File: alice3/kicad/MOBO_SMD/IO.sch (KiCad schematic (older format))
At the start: 31 parts, among them CON1 MicroSD, P2 UART1, P3 USB_OTG, SW2 SOFT RESET, U1 STM32F415RG, Y2 16MHz, Y3 32.768KHz

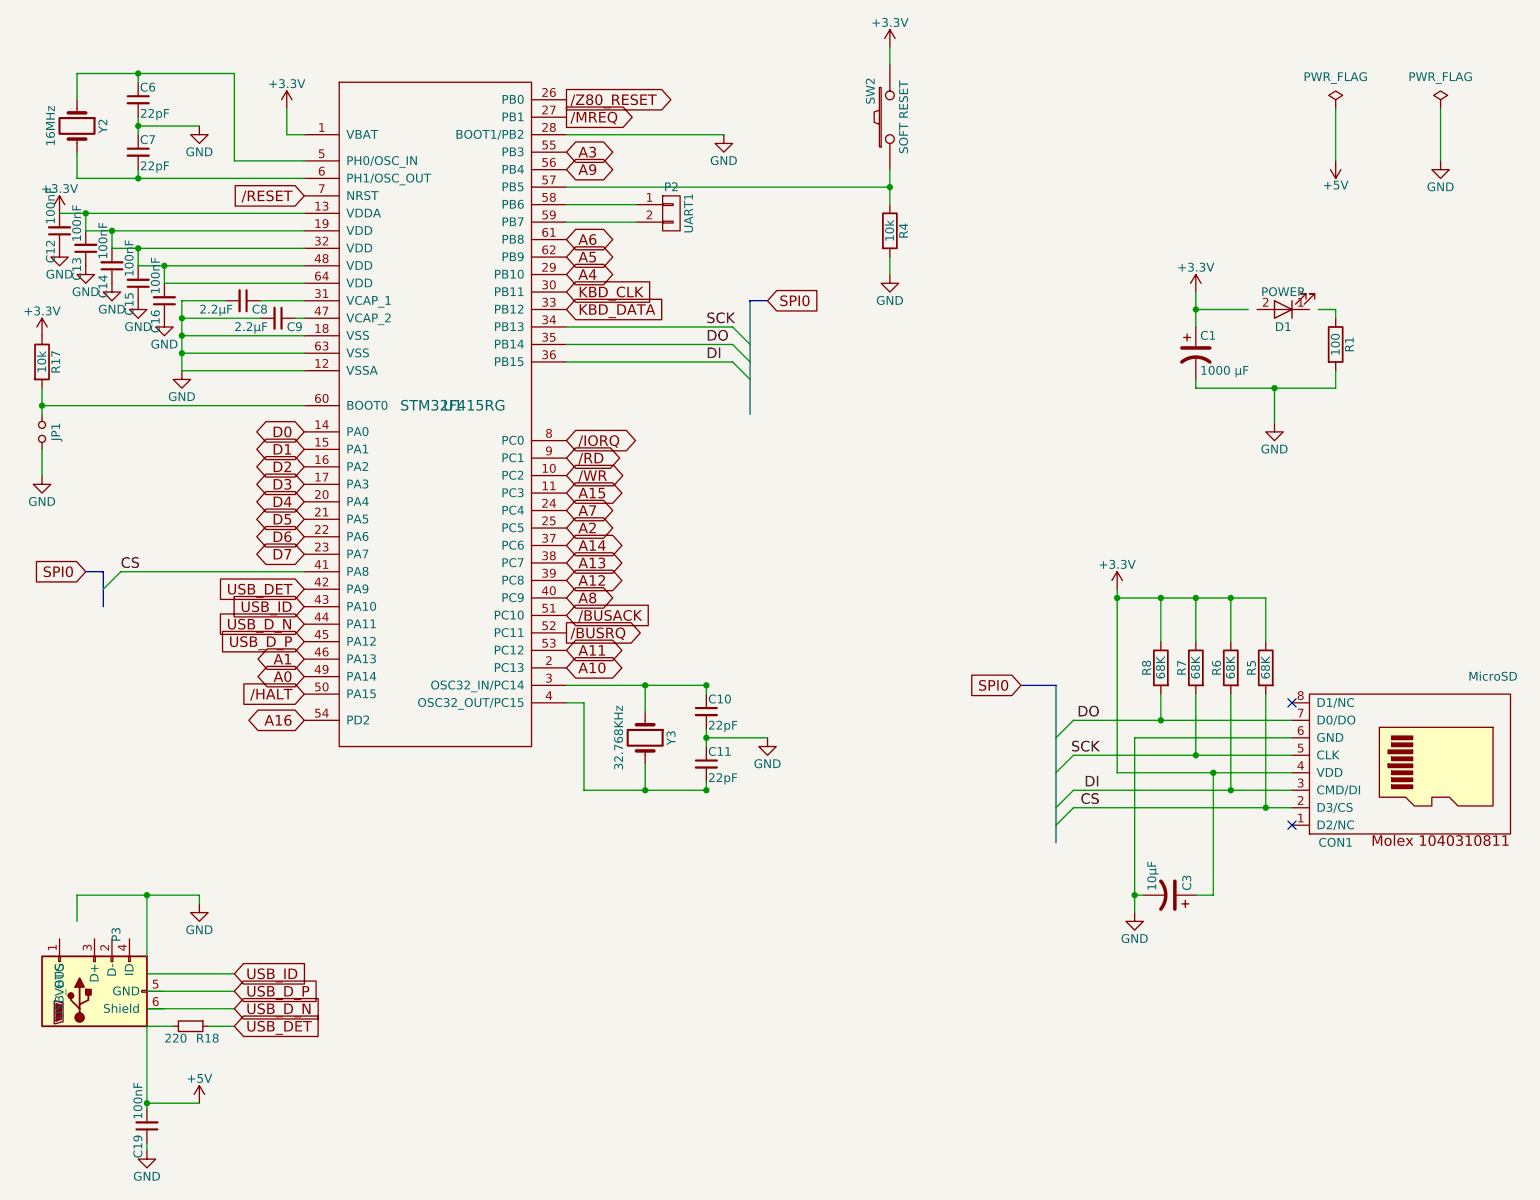
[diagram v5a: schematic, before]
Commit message: Stab at full PCB
replace DIP36 128KB RAM with TSOP44 512KB RAM
change footprints for many components to SMD
sample PCB layout
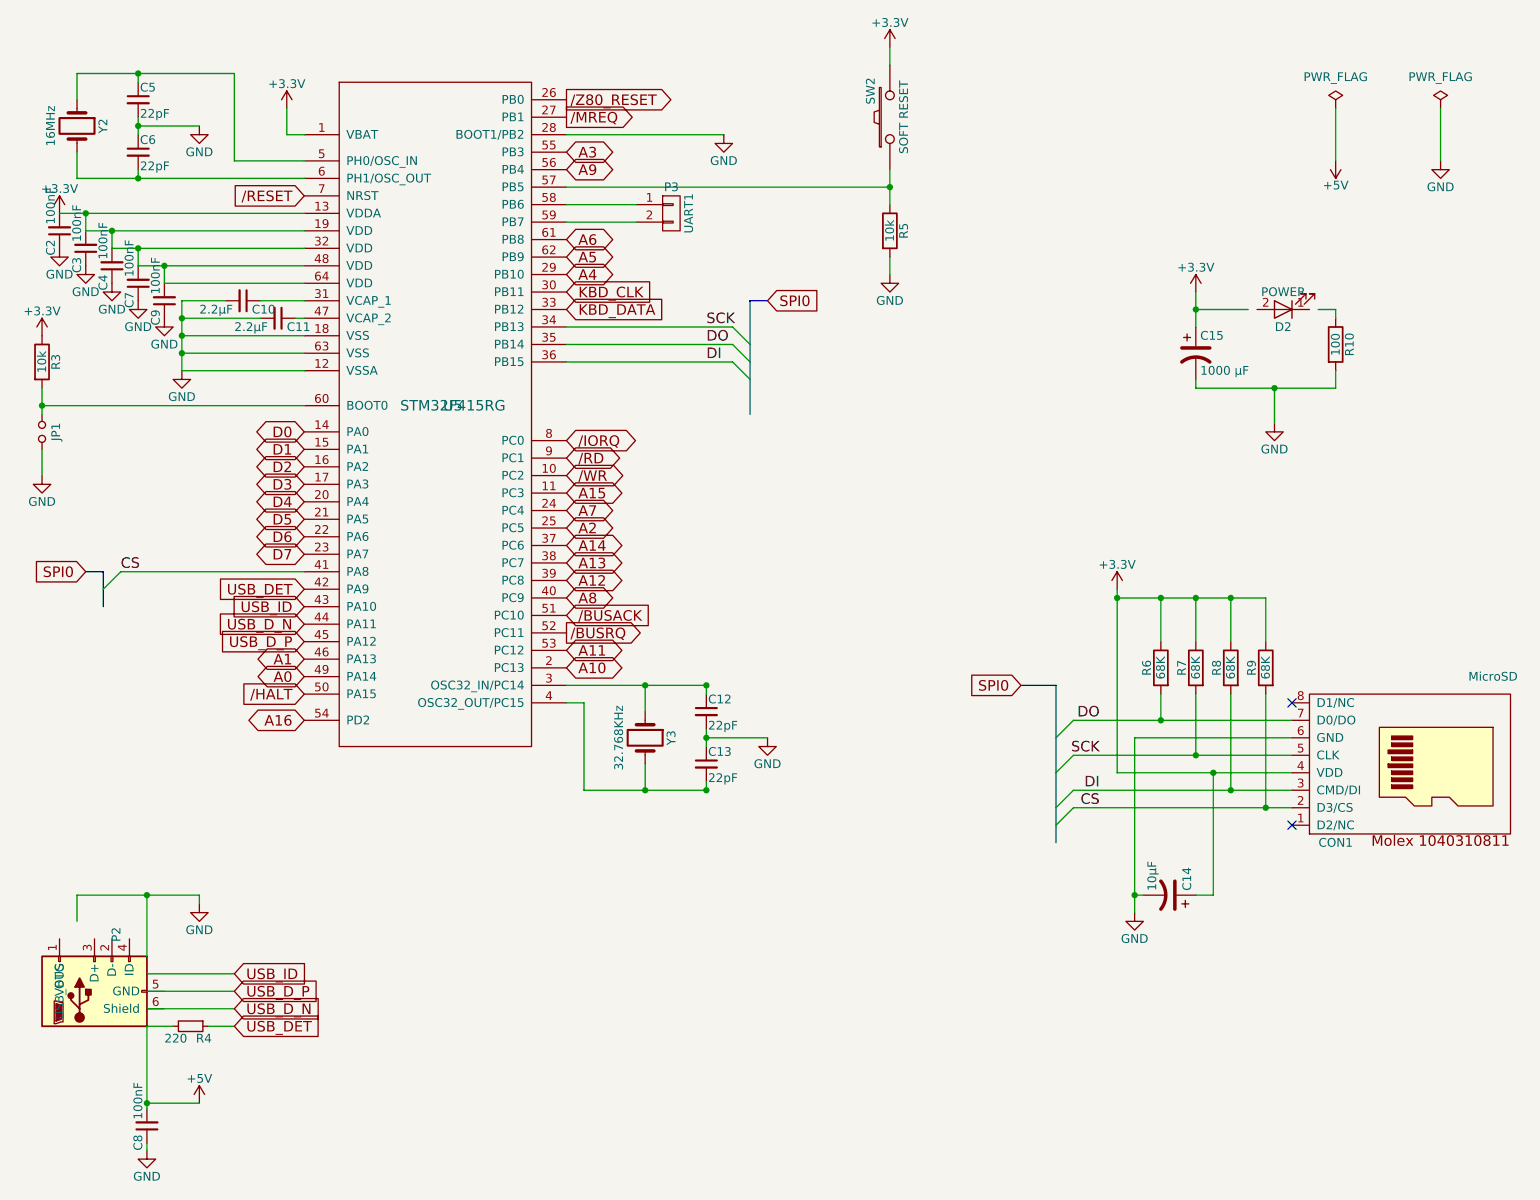
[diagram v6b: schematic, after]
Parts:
- C10: renamed from C8; footprint (none) -> Capacitors_SMD:C_0805
- C11: renamed from C9; footprint (none) -> Capacitors_SMD:C_0805
- C12: renamed from C10; footprint (none) -> Capacitors_SMD:C_0805
- C13: renamed from C11; footprint (none) -> Capacitors_SMD:C_0805
- C2: renamed from C12; footprint (none) -> Capacitors_SMD:C_0805
- C3: renamed from C13; footprint (none) -> Capacitors_SMD:C_0805
- C4: renamed from C14; footprint (none) -> Capacitors_SMD:C_0805
- C5: renamed from C6; footprint (none) -> Capacitors_SMD:C_0805
- C6: renamed from C7; footprint (none) -> Capacitors_SMD:C_0805
- C7: renamed from C15; footprint (none) -> Capacitors_SMD:C_0805
- C8: renamed from C19; footprint (none) -> Capacitors_SMD:C_0805
- C9: renamed from C16; footprint (none) -> Capacitors_SMD:C_0805
- CON1: footprint (none) -> microsd:microsd_socket
- D2: renamed from D1; footprint LEDs:LED-5MM -> LEDs:LED_0805
- JP1: footprint (none) -> Pin_Headers:Pin_Header_Straight_1x02
- P2: renamed from P3; footprint snapeda_conn:10118192-0001LF -> microusb:10118192-0001LF
- P3: renamed from P2; footprint (none) -> Pin_Headers:Pin_Header_Straight_1x02
- R10: renamed from R1; footprint Resistors_ThroughHole:Resistor_Horizontal_RM10mm -> Resistors_SMD:R_0805
- R3: renamed from R17; footprint Resistors_ThroughHole:Resistor_Horizontal_RM10mm -> Resistors_SMD:R_0805
- R4: renamed from R18; footprint (none) -> Resistors_SMD:R_0805
- R5: renamed from R4; footprint Resistors_ThroughHole:Resistor_Horizontal_RM10mm -> Resistors_SMD:R_0805
- R6: renamed from R8; footprint Resistors_ThroughHole:Resistor_Horizontal_RM10mm -> Resistors_SMD:R_0805
- R7: footprint Resistors_ThroughHole:Resistor_Horizontal_RM10mm -> Resistors_SMD:R_0805
- R8: renamed from R6; footprint Resistors_ThroughHole:Resistor_Horizontal_RM10mm -> Resistors_SMD:R_0805
- R9: renamed from R5; footprint Resistors_ThroughHole:Resistor_Horizontal_RM10mm -> Resistors_SMD:R_0805
- Y2, Y3: footprint (none) -> Crystals:Crystal_HC50-U_Vertical
- renumbered C3 to C14, C1 to C15, U1 to U5
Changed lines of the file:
@@
 LIBS:regul
 LIBS:ldo
+LIBS:71v424s15phgi8
 LIBS:MOBO_SMD-cache
 EELAYER 25 0
@@
 $EndComp
 $Comp
-L R R6
+L R R8
 U 1 1 5689A6F4
 P 7700 4500
-F 0 "R6" V 7780 4500 50  0000 C CNN
+F 0 "R8" V 7780 4500 50  0000 C CNN
 F 1 "68K" V 7700 4500 50  0000 C CNN
-F 2 "Resistors_ThroughHole:Resistor_Horizontal_RM10mm" V 7630 4500 30  0001 C CNN
+F 2 "Resistors_SMD:R_0805" V 7630 4500 30  0001 C CNN
 F 3 "" H 7700 4500 30  0000 C CNN
 	1    7700 4500
@@
 $EndComp
 $Comp
-L R R5
+L R R9
 U 1 1 5689A7DE
 P 7900 4500
-F 0 "R5" V 7980 4500 50  0000 C CNN
+F 0 "R9" V 7980 4500 50  0000 C CNN
 F 1 "68K" V 7900 4500 50  0000 C CNN
-F 2 "Resistors_ThroughHole:Resistor_Horizontal_RM10mm" V 7830 4500 30  0001 C CNN
+F 2 "Resistors_SMD:R_0805" V 7830 4500 30  0001 C CNN
 F 3 "" H 7900 4500 30  0000 C CNN
 	1    7900 4500
@@
 F 0 "R7" V 7580 4500 50  0000 C CNN
 F 1 "68K" V 7500 4500 50  0000 C CNN
-F 2 "Resistors_ThroughHole:Resistor_Horizontal_RM10mm" V 7430 4500 30  0001 C CNN
+F 2 "Resistors_SMD:R_0805" V 7430 4500 30  0001 C CNN
 F 3 "" H 7500 4500 30  0000 C CNN
 	1    7500 4500
@@
 $EndComp
 $Comp
-L R R8
+L R R6
 U 1 1 5689A887
 P 7300 4500
-F 0 "R8" V 7380 4500 50  0000 C CNN
+F 0 "R6" V 7380 4500 50  0000 C CNN
 F 1 "68K" V 7300 4500 50  0000 C CNN
-F 2 "Resistors_ThroughHole:Resistor_Horizontal_RM10mm" V 7230 4500 30  0001 C CNN
+F 2 "Resistors_SMD:R_0805" V 7230 4500 30  0001 C CNN
 F 3 "" H 7300 4500 30  0000 C CNN
 	1    7300 4500
@@
 CS
 $Comp
-L R R4
+L R R5
 U 1 1 568A0A99
 P 5750 2000
-F 0 "R4" V 5830 2000 50  0000 C CNN
+F 0 "R5" V 5830 2000 50  0000 C CNN
 F 1 "10k" V 5750 2000 50  0000 C CNN
-F 2 "Resistors_ThroughHole:Resistor_Horizontal_RM10mm" V 5680 2000 30  0001 C CNN
+F 2 "Resistors_SMD:R_0805" V 5680 2000 30  0001 C CNN
 F 3 "" H 5750 2000 30  0000 C CNN
 	1    5750 2000
@@
 $EndComp
 $Comp
-L CP1 C3
+L CP1 C14
 U 1 1 568A9C8C
 P 7350 5800
-F 0 "C3" H 7375 5900 50  0000 L CNN
+F 0 "C14" H 7375 5900 50  0000 L CNN
 F 1 "10µF" H 7375 5700 50  0000 L CNN
 F 2 "Capacitors_ThroughHole:C_Radial_D5_L11_P2.5" H 7350 5800 60  0001 C CNN
@@
 $EndComp
 $Comp
-L CP1 C1
+L CP1 C15
 U 1 1 56A08847
 P 7500 2700
-F 0 "C1" H 7525 2800 50  0000 L CNN
+F 0 "C15" H 7525 2800 50  0000 L CNN
 F 1 "1000 µF" H 7525 2600 50  0000 L CNN
 F 2 "Capacitors_ThroughHole:C_Radial_D8_L11.5_P3.5" H 7500 2700 50  0001 C CNN
@@
 $EndComp
 $Comp
-L LED D1
+L LED D2
 U 1 1 56A0884E
 P 8000 2450
-F 0 "D1" H 8000 2550 50  0000 C CNN
+F 0 "D2" H 8000 2550 50  0000 C CNN
 F 1 "POWER" H 8000 2350 50  0000 C CNN
-F 2 "LEDs:LED-5MM" H 8000 2450 50  0001 C CNN
+F 2 "LEDs:LED_0805" H 8000 2450 50  0001 C CNN
 F 3 "" H 8000 2450 50  0000 C CNN
 	1    8000 2450
@@
 $EndComp
 $Comp
-L R R1
+L R R10
 U 1 1 56A08855
 P 8300 2650
-F 0 "R1" V 8380 2650 50  0000 C CNN
+F 0 "R10" V 8380 2650 50  0000 C CNN
 F 1 "100" V 8300 2650 50  0000 C CNN
-F 2 "Resistors_ThroughHole:Resistor_Horizontal_RM10mm" V 8230 2650 50  0001 C CNN
+F 2 "Resistors_SMD:R_0805" V 8230 2650 50  0001 C CNN
 F 3 "" H 8300 2650 50  0000 C CNN
 	1    8300 2650
@@
 F 0 "Y2" H 1100 1550 50  0000 C CNN
 F 1 "16MHz" H 1100 1250 50  0000 C CNN
-F 2 "" H 1100 1400 60  0001 C CNN
+F 2 "Crystals:Crystal_HC50-U_Vertical" H 1100 1400 60  0001 C CNN
 F 3 "" H 1100 1400 60  0000 C CNN
 	1    1100 1400
@@
 $EndComp
 $Comp
-L C_Small C6
+L C_Small C5
 U 1 1 56BA50E4
 P 1450 1250
-F 0 "C6" H 1460 1320 50  0000 L CNN
+F 0 "C5" H 1460 1320 50  0000 L CNN
 F 1 "22pF" H 1460 1170 50  0000 L CNN
-F 2 "" H 1450 1250 60  0001 C CNN
+F 2 "Capacitors_SMD:C_0805" H 1450 1250 60  0001 C CNN
 F 3 "" H 1450 1250 60  0000 C CNN
 	1    1450 1250
@@
 $EndComp
 $Comp
-L C_Small C7
+L C_Small C6
 U 1 1 56BA5132
 P 1450 1550
-F 0 "C7" H 1460 1620 50  0000 L CNN
+F 0 "C6" H 1460 1620 50  0000 L CNN
 F 1 "22pF" H 1460 1470 50  0000 L CNN
-F 2 "" H 1450 1550 60  0001 C CNN
+F 2 "Capacitors_SMD:C_0805" H 1450 1550 60  0001 C CNN
 F 3 "" H 1450 1550 60  0000 C CNN
 	1    1450 1550
@@
 $EndComp
 $Comp
-L C_Small C8
+L C_Small C10
 U 1 1 56BA543D
 P 2050 2400
-F 0 "C8" V 2100 2450 50  0000 L CNN
+F 0 "C10" V 2100 2450 50  0000 L CNN
 F 1 "2.2µF" V 2100 2150 50  0000 L CNN
-F 2 "" H 2050 2400 60  0001 C CNN
+F 2 "Capacitors_SMD:C_0805" H 2050 2400 60  0001 C CNN
 F 3 "" H 2050 2400 60  0000 C CNN
 	1    2050 2400
@@
 $EndComp
 $Comp
-L C_Small C9
+L C_Small C11
 U 1 1 56BA5533
 P 2250 2500
-F 0 "C9" V 2300 2550 50  0000 L CNN
+F 0 "C11" V 2300 2550 50  0000 L CNN
 F 1 "2.2µF" V 2300 2250 50  0000 L CNN
-F 2 "" H 2250 2500 60  0001 C CNN
+F 2 "Capacitors_SMD:C_0805" H 2250 2500 60  0001 C CNN
 F 3 "" H 2250 2500 60  0000 C CNN
 	1    2250 2500
@@
 $EndComp
 $Comp
-L R R17
+L R R3
 U 1 1 56BA6423
 P 900 2750
-F 0 "R17" V 980 2750 50  0000 C CNN
+F 0 "R3" V 980 2750 50  0000 C CNN
 F 1 "10k" V 900 2750 50  0000 C CNN
-F 2 "Resistors_ThroughHole:Resistor_Horizontal_RM10mm" V 830 2750 30  0001 C CNN
+F 2 "Resistors_SMD:R_0805" V 830 2750 30  0001 C CNN
 F 3 "" H 900 2750 30  0000 C CNN
 	1    900  2750
@@
 F 0 "JP1" H 900 3230 50  0000 C CNN
 F 1 "Jumper_NO_Small" H 910 3090 50  0001 C CNN
-F 2 "" H 900 3150 60  0001 C CNN
+F 2 "Pin_Headers:Pin_Header_Straight_1x02" H 900 3150 60  0001 C CNN
 F 3 "" H 900 3150 60  0000 C CNN
 	1    900  3150
@@
 F 0 "Y3" H 4350 5050 50  0000 C CNN
 F 1 "32.768KHz" H 4350 4750 50  0000 C CNN
-F 2 "" H 4350 4900 60  0001 C CNN
+F 2 "Crystals:Crystal_HC50-U_Vertical" H 4350 4900 60  0001 C CNN
 F 3 "" H 4350 4900 60  0000 C CNN
 	1    4350 4900
@@
 $EndComp
 $Comp
-L C_Small C10
+L C_Small C12
 U 1 1 56BA69CA
 P 4700 4750
-F 0 "C10" H 4710 4820 50  0000 L CNN
+F 0 "C12" H 4710 4820 50  0000 L CNN
 F 1 "22pF" H 4710 4670 50  0000 L CNN
-F 2 "" H 4700 4750 60  0001 C CNN
+F 2 "Capacitors_SMD:C_0805" H 4700 4750 60  0001 C CNN
 F 3 "" H 4700 4750 60  0000 C CNN
 	1    4700 4750
@@
 $EndComp
 $Comp
-L C_Small C11
+L C_Small C13
 U 1 1 56BA69D0
 P 4700 5050
-F 0 "C11" H 4710 5120 50  0000 L CNN
+F 0 "C13" H 4710 5120 50  0000 L CNN
 F 1 "22pF" H 4710 4970 50  0000 L CNN
-F 2 "" H 4700 5050 60  0001 C CNN
+F 2 "Capacitors_SMD:C_0805" H 4700 5050 60  0001 C CNN
 F 3 "" H 4700 5050 60  0000 C CNN
 	1    4700 5050
@@
 F 0 "CON1" H 8300 5500 50  0000 C CNN
 F 1 "MicroSD" H 9200 4550 50  0000 C CNN
-F 2 "" H 9150 5300 50  0001 C CNN
+F 2 "microsd:microsd_socket" H 9150 5300 50  0001 C CNN
 F 3 "" H 8950 4950 50  0000 C CNN
 	1    8750 5050
@@
 $EndComp
 $Comp
-L C_Small C16
+L C_Small C9
 U 1 1 56BAA92C
 P 1600 2400
-F 0 "C16" V 1650 2450 50  0000 L CNN
+F 0 "C9" V 1650 2450 50  0000 L CNN
 F 1 "100nF" V 1650 2150 50  0000 L CNN
-F 2 "" H 1600 2400 60  0001 C CNN
+F 2 "Capacitors_SMD:C_0805" H 1600 2400 60  0001 C CNN
 F 3 "" H 1600 2400 60  0000 C CNN
 	1    1600 2400
@@
 $EndComp
 $Comp
-L C_Small C15
+L C_Small C7
 U 1 1 56BAAAB5
 P 1450 2300
-F 0 "C15" V 1500 2350 50  0000 L CNN
+F 0 "C7" V 1500 2350 50  0000 L CNN
 F 1 "100nF" V 1500 2050 50  0000 L CNN
-F 2 "" H 1450 2300 60  0001 C CNN
+F 2 "Capacitors_SMD:C_0805" H 1450 2300 60  0001 C CNN
 F 3 "" H 1450 2300 60  0000 C CNN
 	1    1450 2300
@@
 $EndComp
 $Comp
-L C_Small C14
+L C_Small C4
 U 1 1 56BAAB11
 P 1300 2200
-F 0 "C14" V 1350 2250 50  0000 L CNN
+F 0 "C4" V 1350 2250 50  0000 L CNN
 F 1 "100nF" V 1350 1950 50  0000 L CNN
-F 2 "" H 1300 2200 60  0001 C CNN
+F 2 "Capacitors_SMD:C_0805" H 1300 2200 60  0001 C CNN
 F 3 "" H 1300 2200 60  0000 C CNN
 	1    1300 2200
@@
 $EndComp
 $Comp
-L C_Small C13
+L C_Small C3
 U 1 1 56BAAB70
 P 1150 2100
-F 0 "C13" V 1200 2150 50  0000 L CNN
+F 0 "C3" V 1200 2150 50  0000 L CNN
 F 1 "100nF" V 1200 1850 50  0000 L CNN
-F 2 "" H 1150 2100 60  0001 C CNN
+F 2 "Capacitors_SMD:C_0805" H 1150 2100 60  0001 C CNN
 F 3 "" H 1150 2100 60  0000 C CNN
 	1    1150 2100
@@
 $EndComp
 $Comp
-L C_Small C12
+L C_Small C2
 U 1 1 56BAABEC
 P 1000 2000
-F 0 "C12" V 1050 2050 50  0000 L CNN
+F 0 "C2" V 1050 2050 50  0000 L CNN
 F 1 "100nF" V 1050 1750 50  0000 L CNN
-F 2 "" H 1000 2000 60  0001 C CNN
+F 2 "Capacitors_SMD:C_0805" H 1000 2000 60  0001 C CNN
 F 3 "" H 1000 2000 60  0000 C CNN
 	1    1000 2000
@@
 Connection ~ 1150 1900
 $Comp
-L CONN_01X02 P2
+L CONN_01X02 P3
 U 1 1 56BAA324
 P 4500 1900
-F 0 "P2" H 4500 2050 50  0000 C CNN
+F 0 "P3" H 4500 2050 50  0000 C CNN
 F 1 "UART1" V 4600 1900 50  0000 C CNN
-F 2 "" H 4500 1900 60  0001 C CNN
+F 2 "Pin_Headers:Pin_Header_Straight_1x02" H 4500 1900 60  0001 C CNN
 F 3 "" H 4500 1900 60  0000 C CNN
 	1    4500 1900
@@
 	3900 1950 4300 1950
 $Comp
-L USB_OTG P3
+L USB_OTG P2
 U 1 1 56BAA76F
 P 1200 6350
-F 0 "P3" H 1525 6225 50  0000 C CNN
+F 0 "P2" H 1525 6225 50  0000 C CNN
 F 1 "USB_OTG" H 1200 6550 50  0000 C CNN
-F 2 "snapeda_conn:10118192-0001LF" V 1150 6250 60  0001 C CNN
+F 2 "microusb:10118192-0001LF" V 1150 6250 60  0001 C CNN
 F 3 "" V 1150 6250 60  0000 C CNN
 	1    1200 6350
@@
 $EndComp
 $Comp
-L STM32F415RG U?
+L STM32F415RG U5
 U 1 1 56B635D1
 P 3250 3000
-AR Path="/56B635D1" Ref="U?"  Part="1"
-AR Path="/568DBAE1/56B635D1" Ref="U1"  Part="1"
-F 0 "U1" H 3250 3000 60  0000 C CNN
+F 0 "U5" H 3250 3000 60  0000 C CNN
 F 1 "STM32F415RG" H 3250 3000 60  0000 C CNN
 F 2 "Housings_QFP:LQFP-64_10x10mm_Pitch0.5mm" H 3250 3000 60  0001 C CNN
@@
 	1800 5800 1800 5850
 $Comp
-L R_Small R18
+L R_Small R4
 U 1 1 56BAC147
 P 1750 6550
-F 0 "R18" V 1820 6580 50  0000 L CNN
+F 0 "R4" V 1820 6580 50  0000 L CNN
 F 1 "220" V 1820 6400 50  0000 L CNN
-F 2 "" H 1750 6550 60  0001 C CNN
+F 2 "Resistors_SMD:R_0805" H 1750 6550 60  0001 C CNN
 F 3 "" H 1750 6550 60  0000 C CNN
 	1    1750 6550
@@
 $EndComp
 $Comp
-L C_Small C19
+L C_Small C8
 U 1 1 56BAC974
 P 1500 7120
-F 0 "C19" V 1550 7170 50  0000 L CNN
+F 0 "C8" V 1550 7170 50  0000 L CNN
 F 1 "100nF" V 1550 6870 50  0000 L CNN
-F 2 "" H 1500 7120 60  0001 C CNN
+F 2 "Capacitors_SMD:C_0805" H 1500 7120 60  0001 C CNN
 F 3 "" H 1500 7120 60  0000 C CNN
 	1    1500 7120

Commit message: set crystals to SMD footprints
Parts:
- Y2: footprint Crystals:Crystal_HC50-U_Vertical -> Crystals:ABM3
- Y3: footprint Crystals:Crystal_HC50-U_Vertical -> Resistors_SMD:R_0805
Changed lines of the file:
@@
 F 0 "Y2" H 1100 1550 50  0000 C CNN
 F 1 "16MHz" H 1100 1250 50  0000 C CNN
-F 2 "Crystals:Crystal_HC50-U_Vertical" H 1100 1400 60  0001 C CNN
+F 2 "Crystals:ABM3" H 1100 1400 60  0001 C CNN
 F 3 "" H 1100 1400 60  0000 C CNN
 	1    1100 1400
@@
 F 0 "Y3" H 4350 5050 50  0000 C CNN
 F 1 "32.768KHz" H 4350 4750 50  0000 C CNN
-F 2 "Crystals:Crystal_HC50-U_Vertical" H 4350 4900 60  0001 C CNN
+F 2 "Resistors_SMD:R_0805" H 4350 4900 60  0001 C CNN
 F 3 "" H 4350 4900 60  0000 C CNN
 	1    4350 4900

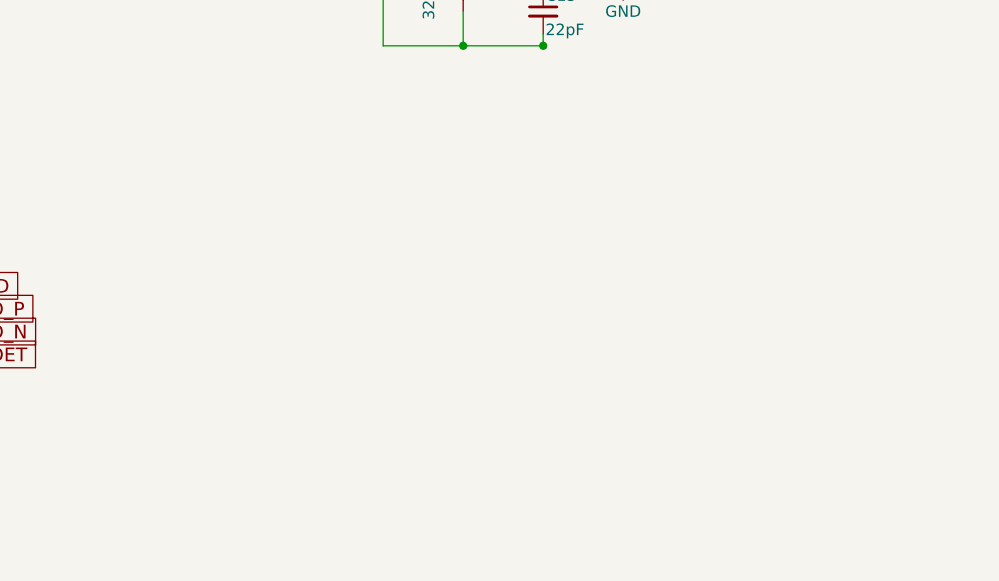
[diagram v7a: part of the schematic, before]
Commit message: interpolate VGA and PS/2 from Parallax board
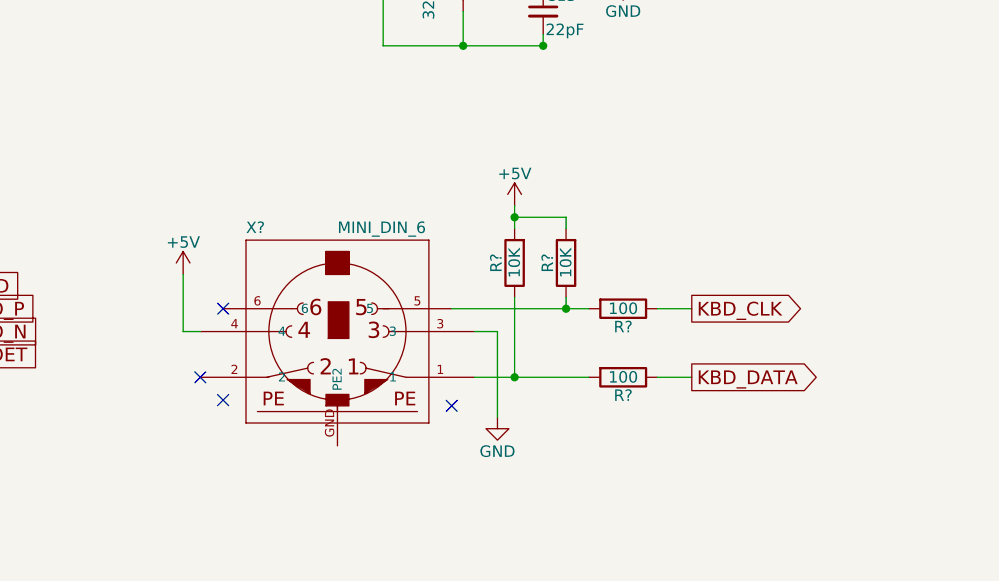
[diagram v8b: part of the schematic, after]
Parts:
- added R? (x2): 100, symbol R
- added R? (x2): 10K, symbol R
- added X?: MINI_DIN_6, mini_din-M_DIN6, symbol MINI_DIN_6
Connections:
- wire segments 95 -> 108
- no-connect marks 2 -> 6
